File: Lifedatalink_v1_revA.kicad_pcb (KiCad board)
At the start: 2 copper layers, 48.3 x 40 mm, 64 parts, among them J1 DX07S024XJ1R1100, J2 BATTERY CONNECTOR, J3 DF17(4.0)-30DS-0.5V(57), J4 503480-0600, Q1 DMG2301L, U1 BL654, U2 LP5907MFX-3_3_NOPB, U3 ADS1292R, U4 MCP73831-2-OT, U5 TMP117NAIYBGR, U6 MAX30102, U7 LP5907MFX-1.8, Y1 Crystal

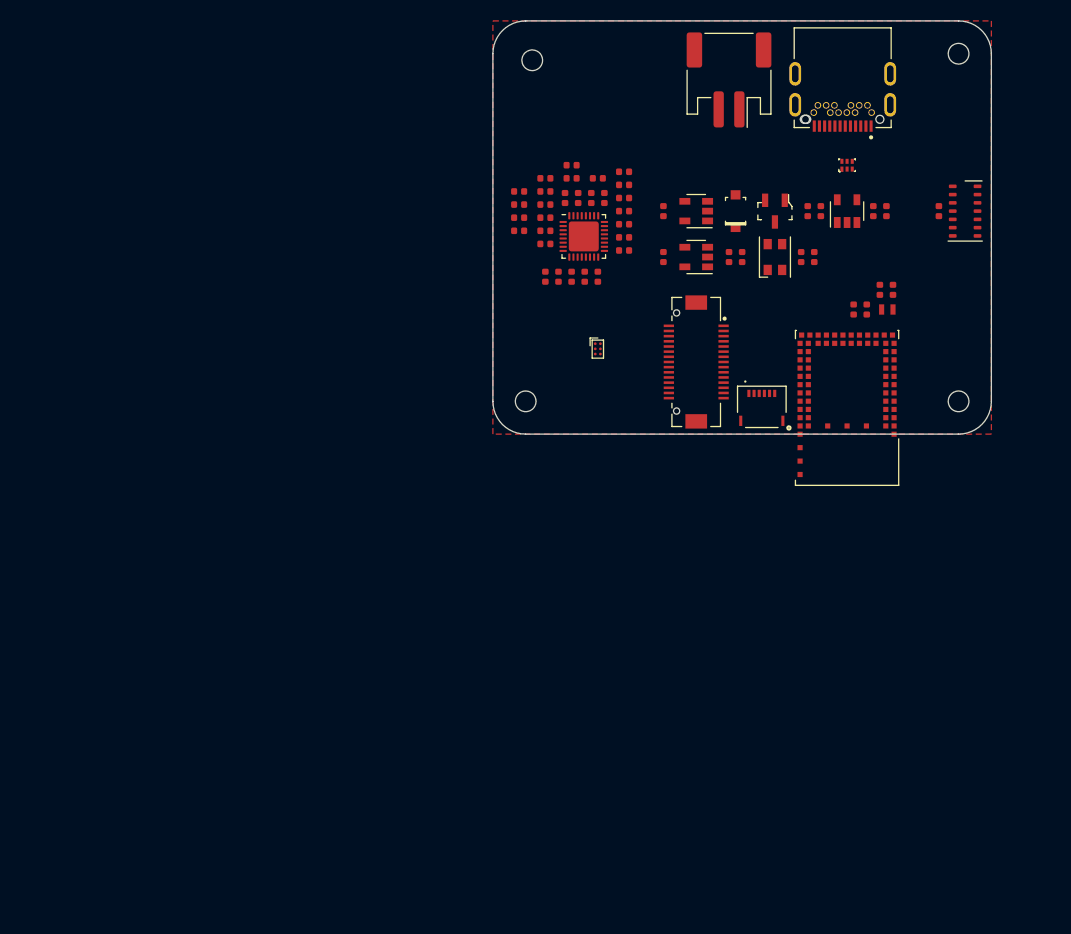
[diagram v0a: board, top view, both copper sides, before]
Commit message: Hexagonal PCB placed
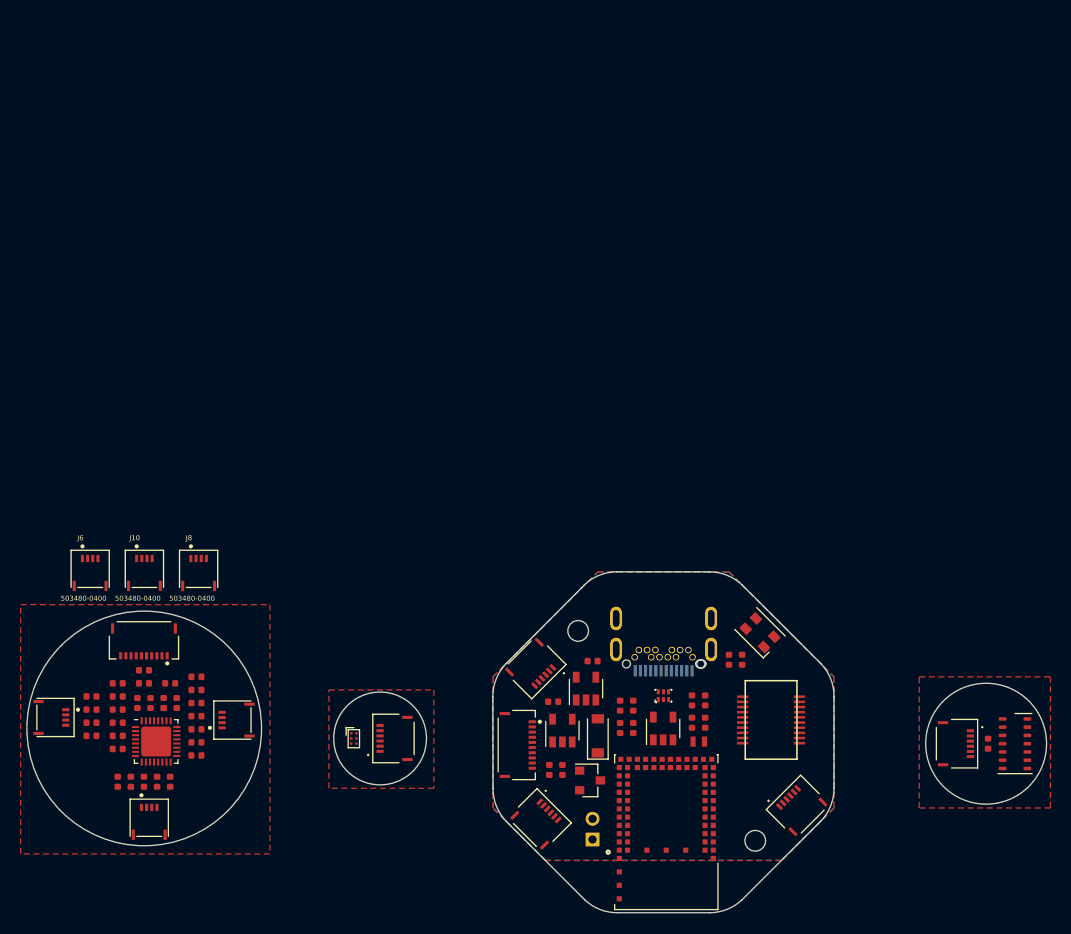
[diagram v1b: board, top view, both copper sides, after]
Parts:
- removed the REF** at (155.6, 102.9)
- removed the REF** at (156.2, 69.8)
- added J10: 503480-0400, 503480-0400:MOLEX_503480-0400, F.Cu at (118.7, 119.4)
- added J11: 5034801000, MOLEX_503480-0600:MOLEX_5034801000, F.Cu at (118.6, 127.5)
- added J12: 5034801000, MOLEX_503480-0600:MOLEX_5034801000, F.Cu at (156.2, 136.1)
- added J13: 503480-0600, MOLEX_503480-0600:MOLEX_503480-0600, F.Cu at (142.9, 135.5)
- added J14: 503480-0600, MOLEX_503480-0600:MOLEX_503480-0600, F.Cu at (156.3, 128.5)
- added J15: 503480-0600, MOLEX_503480-0600:MOLEX_503480-0600, F.Cu at (182.0, 142.2)
- added J16: 503480-0600, MOLEX_503480-0600:MOLEX_503480-0600, F.Cu at (197.2, 136.0)
- added J5: 503480-0400, 503480-0400:MOLEX_503480-0400, F.Cu at (127.5, 133.7)
- added J6: 503480-0400, 503480-0400:MOLEX_503480-0400, F.Cu at (113.4, 119.4)
- added J7: 503480-0400, 503480-0400:MOLEX_503480-0400, F.Cu at (109.7, 133.5)
- added J8: 503480-0400, 503480-0400:MOLEX_503480-0400, F.Cu at (123.9, 119.4)
- added J9: 503480-0400, 503480-0400:MOLEX_503480-0400, F.Cu at (119.1, 143.5)
- D3: footprint digikey-footprints:SOD-123 -> Diode_SMD:D_SOD-123
- J1: moved to B.Cu
- J2: footprint Connector_JST:JST_PH_S2B-PH-SM4-TB_1x02-1MP_P2.00mm_Horizontal -> Connector_PinHeader_2.00mm:PinHeader_1x02_P2.00mm_Vertical; moved to B.Cu
- J3: value DF17(4.0)-30DS-0.5V(57) -> Conn_02x10_Odd_Even; footprint HRS_DF17(4.0)-30DS-0:HRS_DF17(4.0)-30DS-0.5V(57) -> DF23:DF23C-20DS-0.5V(51)
- Q1: footprint digikey-footprints:SOT-23-3 -> Package_TO_SOT_SMD:SOT-23
- moved REF** 78.7 mm to (177.8, 145.4)
- moved J2 74.7 mm to (162.1, 145.3), turned to 0 degrees
- moved C19 64.1 mm to (120.5, 132.1)
- moved R12 64.1 mm to (118.6, 130.2)
- moved C12 64.1 mm to (123.7, 132.1)
- moved C15 64.1 mm to (113.5, 132.7)
- moved C16 64.1 mm to (113.5, 134.0)
- moved C18 64.1 mm to (119.3, 132.1)
- moved C22 64.1 mm to (123.7, 134.6)
- moved R13 64.1 mm to (121.2, 130.2)
- moved R14 64.1 mm to (118.6, 128.9)
- moved C11 64.1 mm to (118.6, 139.7)
- moved C13 64.1 mm to (116.1, 135.3)
- moved C14 64.1 mm to (116.1, 136.5)
- moved C17 64.1 mm to (113.5, 135.3)
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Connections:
- U1 pad 12: Net-(J3-Pad22) -> Net-(J3-Pad20)
- U1 pad 13: Net-(J3-Pad20) -> Net-(J3-Pad18)
- U1 pad 14: Net-(J3-Pad18) -> Net-(J3-Pad16)
- U1 pad 16: Net-(J3-Pad14) -> Net-(J3-Pad12)
- U1 pad 18: Net-(J3-Pad10) -> Net-(J3-Pad8)
- U1 pad 19: Net-(J3-Pad16) -> Net-(J3-Pad14)
- U1 pad 20: Net-(J3-Pad6) -> Net-(J3-Pad4)
- U1 pad 21: Net-(J3-Pad12) -> Net-(J3-Pad10)
- U1 pad 22: Net-(J3-Pad8) -> Net-(J3-Pad6)
- U1 pad 27: Net-(J3-Pad2) -> Net-(U1-Pad27)
- U1 pad 28: Net-(J3-Pad4) -> Net-(J3-Pad2)
- U1 pad 44: Net-(U1-Pad44) -> /TMP_ADD0
- U5 pad C1: GND -> /TMP_ADD0
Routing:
- added copper zone on B.Cu, net GND
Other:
- board size 48.3 x 40 mm -> 98.7 x 33 mm

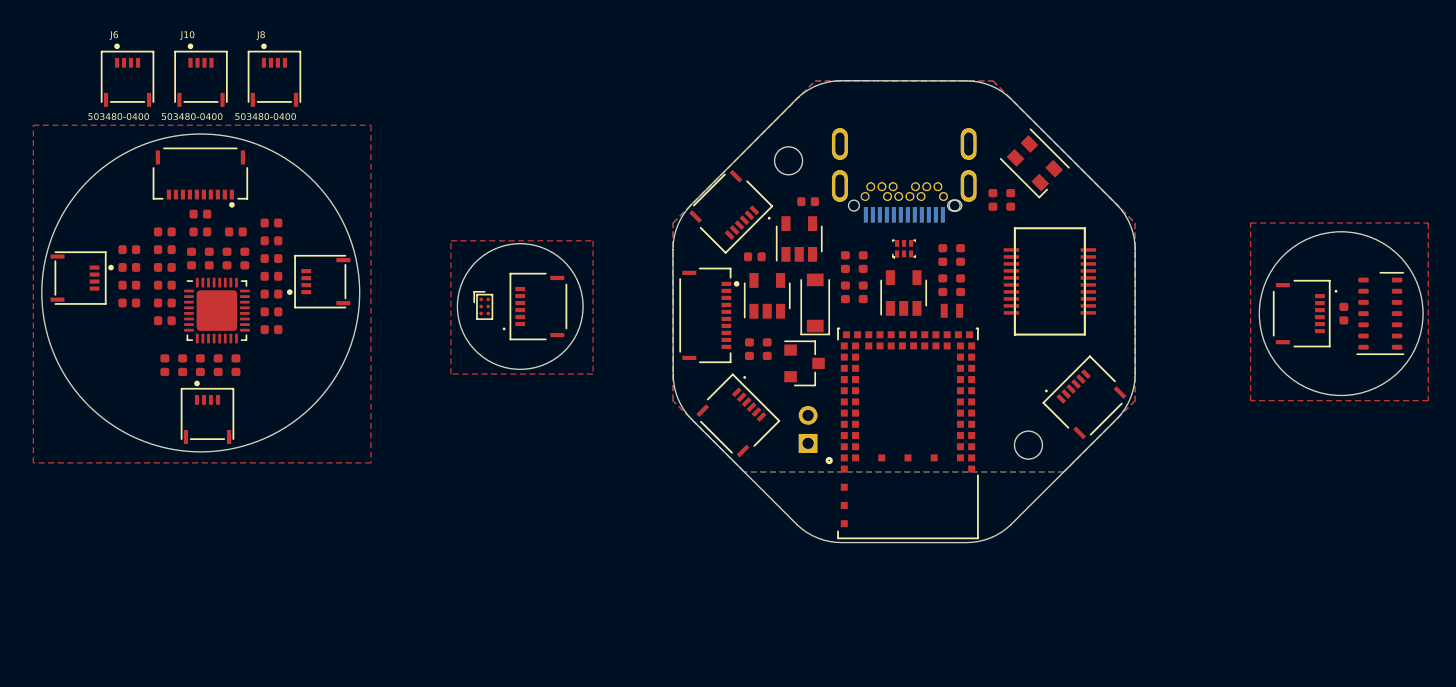
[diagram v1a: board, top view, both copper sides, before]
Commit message: Cutted PCB placed and 3D models added
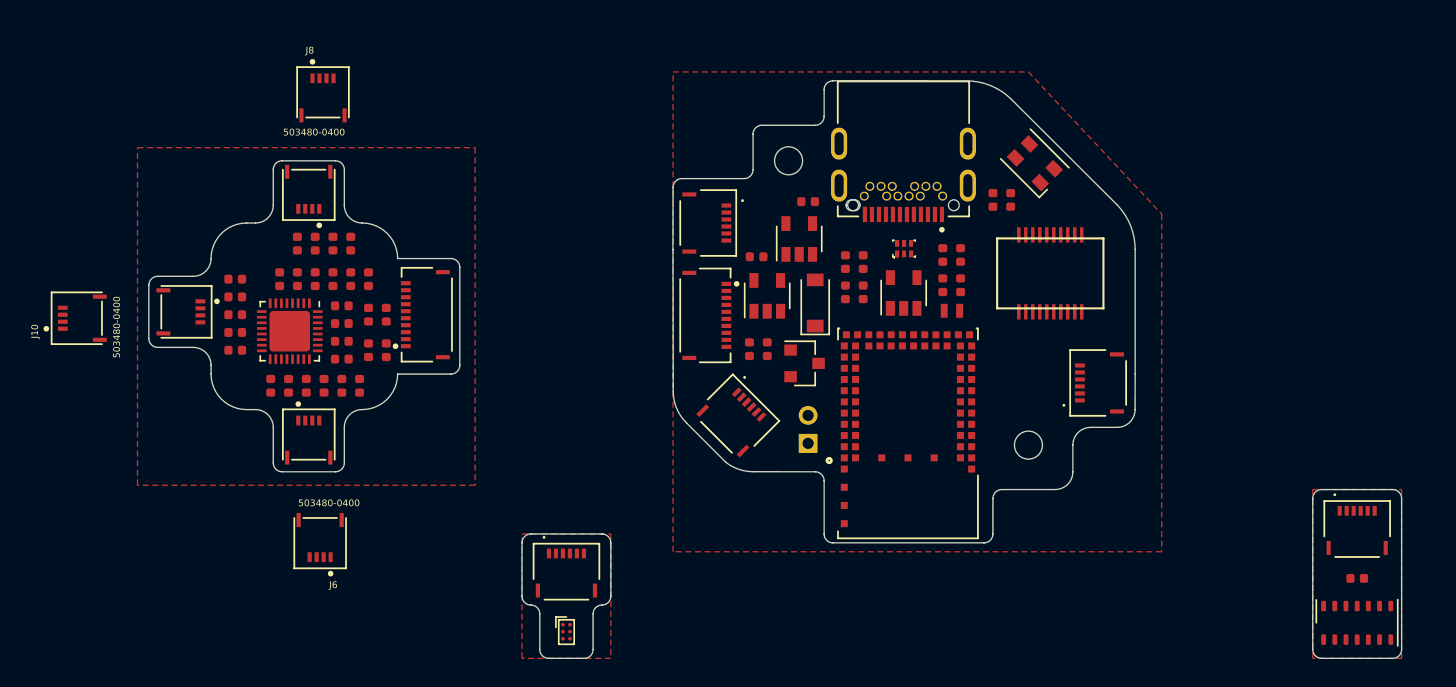
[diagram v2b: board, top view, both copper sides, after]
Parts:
- added BAT: 401030, Battery:401030, B.Cu at (168.9, 135.9)
- J1: moved to F.Cu
- moved J6 35.5 mm to (127.2, 152.1), turned to 180 degrees
- moved U5 24.0 mm to (144.8, 158.8)
- moved U6 22.2 mm to (201.3, 158.1), turned to 90 degrees
- moved J13 19.1 mm to (144.8, 154.6), turned to 0 degrees
- moved J10 19.0 mm to (110.1, 136.3), turned to 90 degrees
- moved C24 18.9 mm to (201.3, 154.9), turned to 0 degrees
- moved J7 17.8 mm to (126.4, 127.2), turned to 180 degrees
- moved J11 17.0 mm to (133.3, 136.1), turned to 90 degrees
- moved J16 16.0 mm to (201.3, 151.5), turned to 0 degrees
- moved R5 15.8 mm to (129.4, 131.0), turned to 90 degrees
- moved R14 15.1 mm to (131.9, 136.1), turned to 90 degrees
- moved C21 14.9 mm to (130.6, 133.6), turned to 90 degrees
- moved C15 14.7 mm to (128.1, 131.0), turned to 270 degrees
- moved C16 13.6 mm to (126.8, 131.0), turned to 90 degrees
- moved R11 13.5 mm to (129.4, 133.6), turned to 90 degrees
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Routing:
- removed copper zone on B.Cu, net GND
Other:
- board size 98.7 x 33 mm -> 89.5 x 41.3 mm

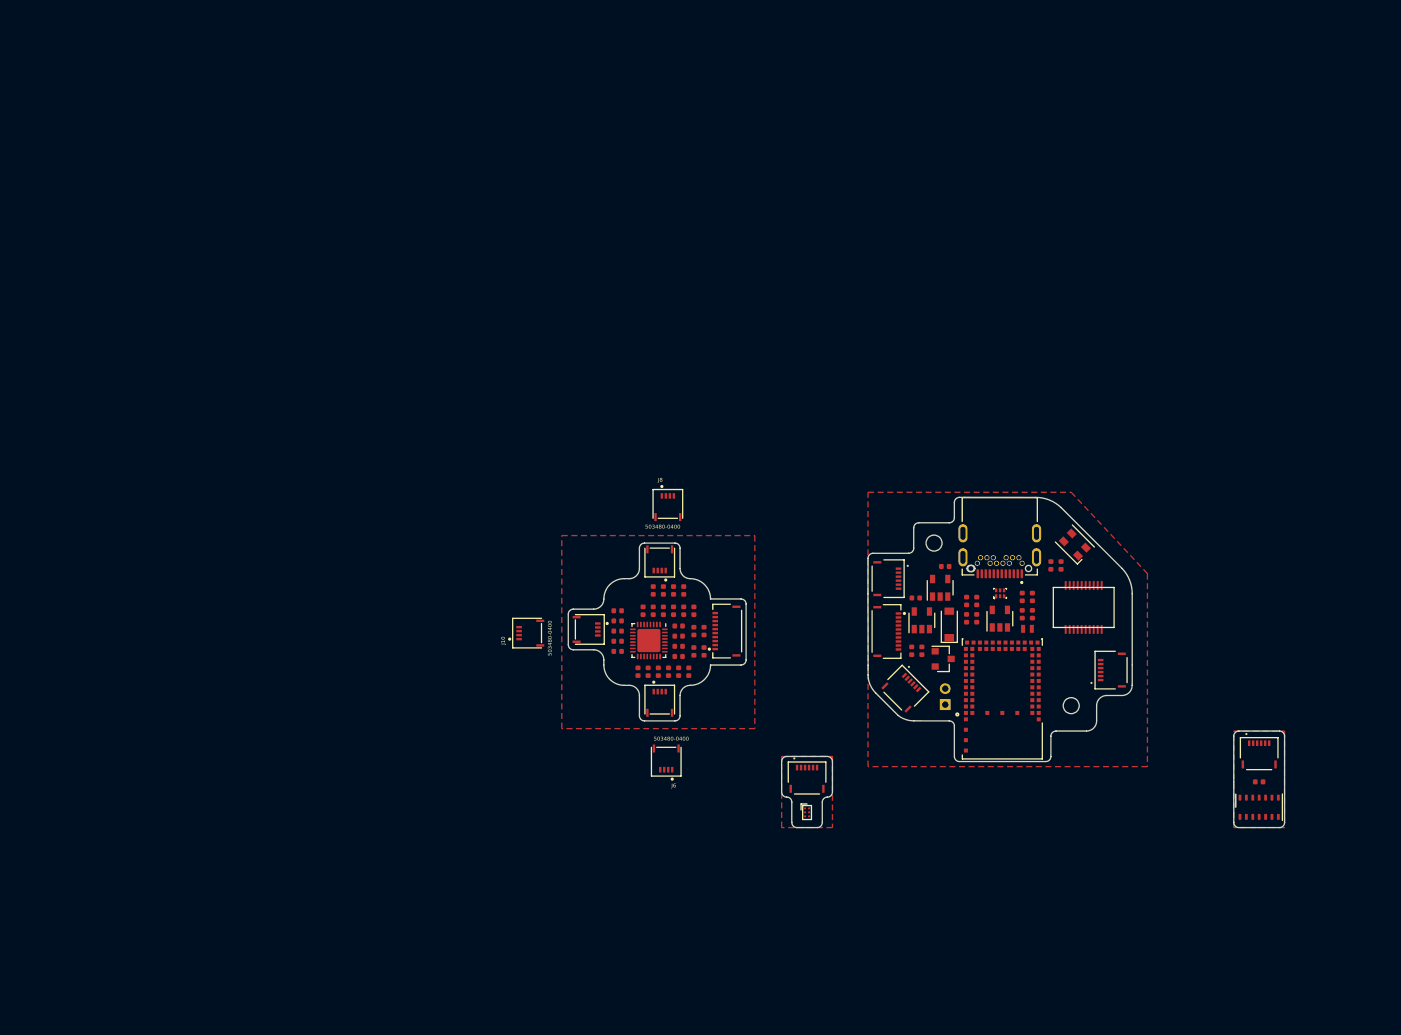
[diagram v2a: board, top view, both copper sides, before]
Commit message: Added ECG snaps, microphones and other 3D models.
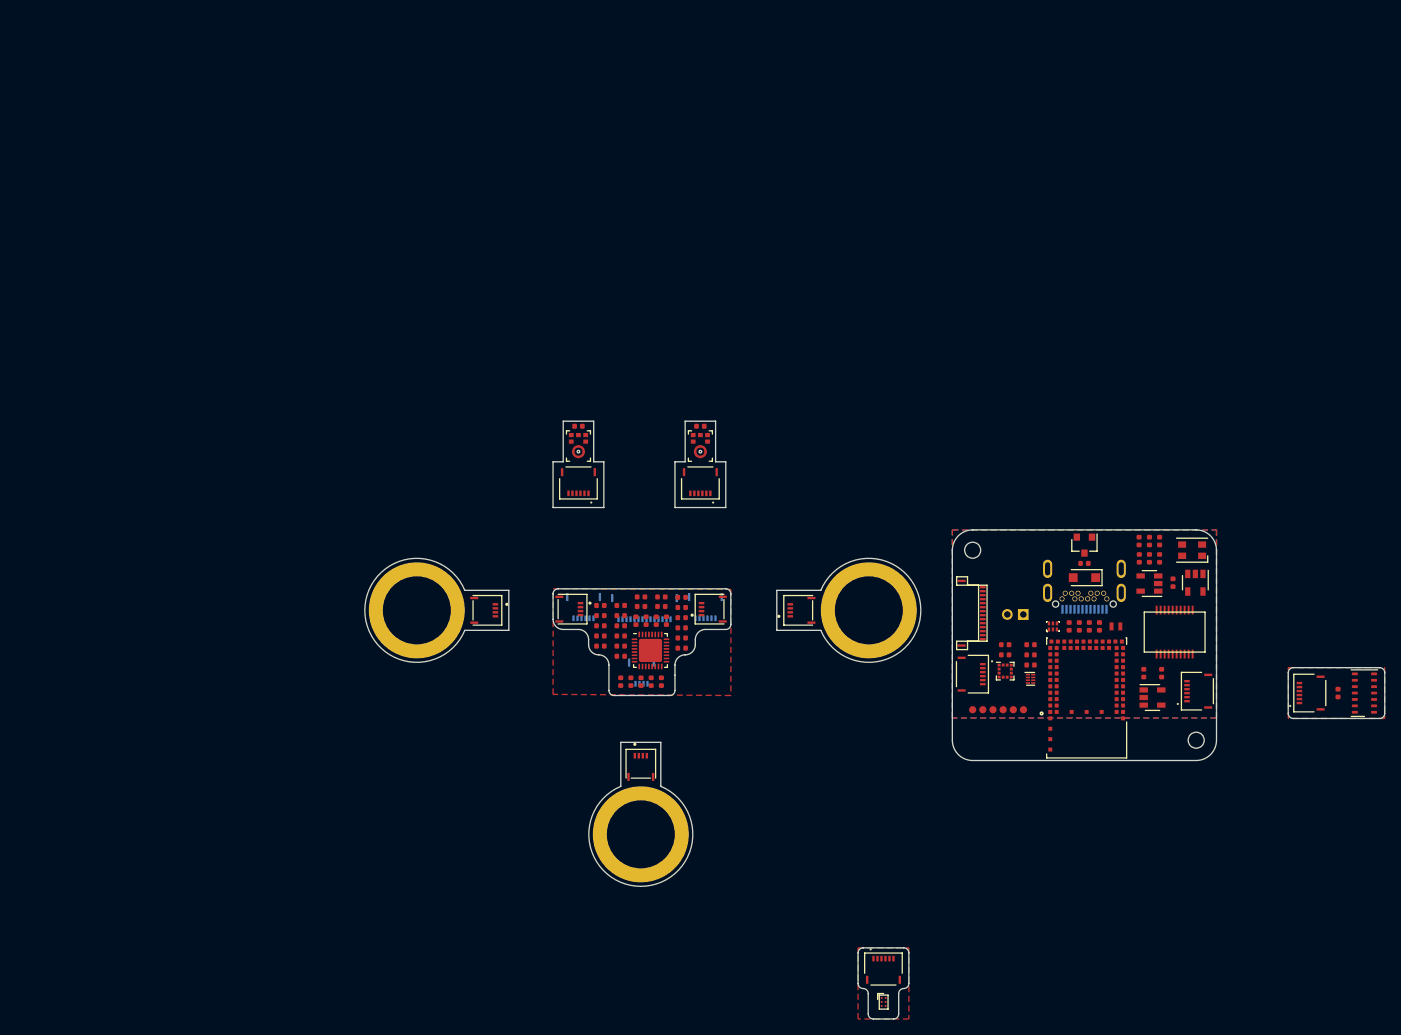
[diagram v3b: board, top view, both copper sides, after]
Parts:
- added C27: 100nF, Capacitor_SMD:C_0402_1005Metric, F.Cu at (169.5, 137.8)
- added C28: 10uF, Capacitor_SMD:C_0402_1005Metric, F.Cu at (169.5, 139.1)
- added C29: 0.1uF, Capacitor_SMD:C_0402_1005Metric, F.Cu at (116.2, 110.5)
- added C30: 0.1uF, Capacitor_SMD:C_0402_1005Metric, F.Cu at (131.4, 110.5)
- added J17: 503480-0600, MOLEX_503480-0600:MOLEX_503480-0600, B.Cu at (132.1, 133.1)
- added J18: 503480-0600, MOLEX_503480-0600:MOLEX_503480-0600, F.Cu at (116.2, 117.5)
- added J19: 503480-0600, MOLEX_503480-0600:MOLEX_503480-0600, F.Cu at (131.4, 117.5)
- added J20: 503480-0600, MOLEX_503480-0600:MOLEX_503480-0600, B.Cu at (116.8, 133.1)
- added MIC1: ICS-43434, digikey-footprints:SPH0645LM4H-B, F.Cu at (116.2, 113.7)
- added MIC2: ICS-43434, digikey-footprints:SPH0645LM4H-B, F.Cu at (131.4, 113.7)
- added R17: 200K, Resistor_SMD:R_0402_1005Metric, F.Cu at (172.7, 137.8)
- added R20: 4.7K, Resistor_SMD:R_0402_1005Metric, F.Cu at (172.7, 140.3)
- added R21: 4.7K, Resistor_SMD:R_0402_1005Metric, F.Cu at (172.7, 139.1)
- added R22: 100K, Resistor_SMD:R_0402_1005Metric, F.Cu at (118.9, 132.9)
- added REF**: ECG_SNAP, MOLEX_503480-0600:ECG_SNAP, F.Cu at (124.0, 161.5)
- added REF**: ECG_SNAP, MOLEX_503480-0600:ECG_SNAP, F.Cu at (96.0, 133.5)
- added REF**: ECG_SNAP, MOLEX_503480-0600:ECG_SNAP, F.Cu at (152.5, 133.5)
- added U8: IIS2DLPCTR, Package_LGA:LGA-12_2x2mm_P0.5mm, F.Cu at (169.5, 141.1)
- added U9: PCA9306, Package_SON:X2SON-8_1.4x1mm_P0.35mm, F.Cu at (172.7, 142.1)
- D3: footprint Diode_SMD:D_SOD-123 -> Diode_SMD:D_SOD-123F
- J1, J9: moved to B.Cu
- J11: value 5034801000 -> 5034801400; footprint MOLEX_503480-0600:MOLEX_5034801000 -> MOLEX_503480-0600:5034801400; moved to B.Cu
- J12: value 5034801000 -> 5034801400; footprint MOLEX_503480-0600:MOLEX_5034801000 -> MOLEX_503480-0600:5034801400
- J4: value 503480-0600 -> Conn_01x06; footprint MOLEX_503480-0600:MOLEX_503480-0600 -> Pads_1.27mm:1.27mm_pads_01x06
- moved C26 32.1 mm to (189.1, 141.4), turned to 270 degrees
- moved C3 30.7 mm to (187.6, 127.0)
- moved U7 30.4 mm to (188.0, 144.4), turned to 0 degrees
- moved C25 29.1 mm to (186.9, 141.4)
- moved J8 26.3 mm to (104.5, 133.5), turned to 270 degrees
- moved U2 26.2 mm to (187.6, 130.1), turned to 180 degrees
- moved J13 25.7 mm to (154.3, 178.4)
- moved U5 25.6 mm to (154.4, 182.4)
- moved J6 25.1 mm to (144.0, 133.5), turned to 90 degrees
- moved R3 24.9 mm to (190.5, 130.0)
- moved U4 24.8 mm to (193.3, 130.0), turned to 270 degrees
- moved C4 24.3 mm to (186.3, 127.0), turned to 90 degrees
- moved Q1 22.7 mm to (179.5, 125.3), turned to 270 degrees
- moved J10 21.7 mm to (124.0, 153.0), turned to 0 degrees
- moved U6 19.4 mm to (214.5, 143.8), turned to 180 degrees
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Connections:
- C26 pad 1: GND -> Net-(C26-Pad1)
- J11 pad 10: GND -> Net-(J11-Pad10)
- J12 pad 10: GND -> Net-(J12-Pad10)
- J13 pad 2: /BL654_I2C_SCL -> /BL654_I2C_SCL_HV
- J13 pad 3: /BL654_I2C_SDA -> /BL654_I2C_SDA_HV
- J14 pad 2: /BL654_I2C_SCL -> /BL654_I2C_SCL_HV
- J14 pad 3: /BL654_I2C_SDA -> /BL654_I2C_SDA_HV
- J15 pad 2: /BL654_I2C_SCL -> +1V8
- J15 pad 3: /BL654_I2C_SDA -> /BL654_I2C_SCL_LV
- J15 pad 4: /~MAX_INT -> /BL654_I2C_SDA_LV
- J15 pad 5: Net-(J15-Pad5) -> /~MAX_INT
- J16 pad 2: /BL654_I2C_SCL -> +1V8
- J16 pad 3: /BL654_I2C_SDA -> /BL654_I2C_SCL_LV
- J16 pad 4: /~MAX_INT -> /BL654_I2C_SDA_LV
- J16 pad 5: Net-(J16-Pad5) -> /~MAX_INT
- J3 pad 1: Net-(J3-Pad1) -> +5V
- R18 pad 2: /BL654_I2C_SCL -> /BL654_I2C_SDA_HV
- R19 pad 2: /BL654_I2C_SDA -> /BL654_I2C_SCL_HV
- U1 pad 10: Net-(U1-Pad10) -> /BL654_I2S_SCK
- U1 pad 36: /BL654_I2C_SDA -> /BL654_I2C_SDA_HV
- U1 pad 38: /BL654_I2C_SCL -> /BL654_I2C_SCL_HV
- U1 pad 8: Net-(U1-Pad8) -> /BL654_I2S_WS
- U1 pad 9: Net-(U1-Pad9) -> /BL654_I2S_SD
- U5 pad A1: /BL654_I2C_SDA -> /BL654_I2C_SDA_HV
- U5 pad A2: /BL654_I2C_SCL -> /BL654_I2C_SCL_HV
- U6 pad 2: /BL654_I2C_SCL -> /BL654_I2C_SCL_LV
- U6 pad 3: /BL654_I2C_SDA -> /BL654_I2C_SDA_LV
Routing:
- added copper zone on B.Cu, net GND
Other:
- board size 89.5 x 41.3 mm -> 127.5 x 74.7 mm
